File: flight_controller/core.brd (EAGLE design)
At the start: 94 x 90 mm, 103 parts, among them J1 M02, J13 MOLEX-3POS, J14 MOLEX-3POS, J15 MOLEX-4POS, J16 MOLEX-3POS, J17 M03, J18 M04, J19 MOLEX-3POS, J2 MOLEX-2POS, J20 MOLEX-4POS, J3 MOLEX-2POS, J4 MOLEX-2POS, J5 MOLEX-2POS, J6 MOLEX-2POS, J7 MOLEX-2POS, J8 MOLEX-2POS, J9 MOLEX-2POS, Q10 EM6K1, Q11 EM6K1, Q2 200mA/50V, Q5 200mA/50V, Q6 200mA/50V, Q7 EM6K1, Q8 EM6K1, U1 MPU-6000QFN-24, U2 MEAS-MS5611, U3 USD-SOCKETNEW, U4 STM32F405, U5 MIC5219 3.3V, Y1 16MHz

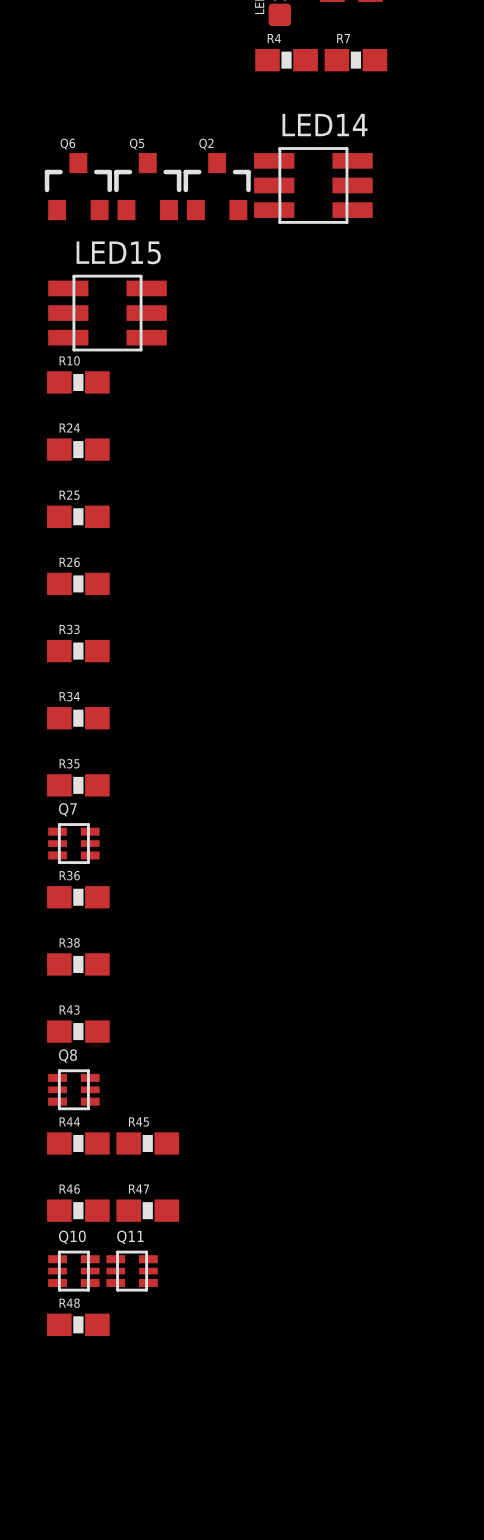
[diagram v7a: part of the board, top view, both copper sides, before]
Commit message: Replace LED MOSFETs with dual-channel MOSFETs.
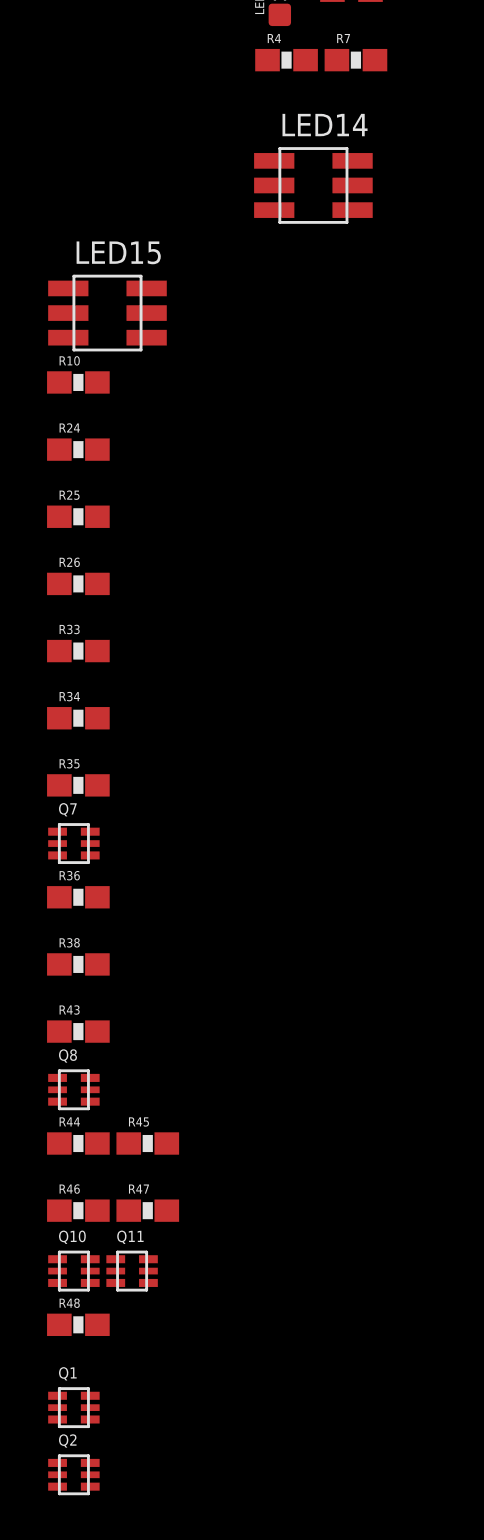
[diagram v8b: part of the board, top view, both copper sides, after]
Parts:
- removed Q5, Q6: 200mA/50V, SparkFun-DiscreteSemi:SOT23-3
- added Q1: EM6K1, OSURC_DiscreteSemi:SOT-666
- Q2: value 200mA/50V -> EM6K1; device SparkFun-DiscreteSemi:SOT23-3 -> OSURC_DiscreteSemi:SOT-666
- moved Q2 57.9 mm to (-224.0, -588.9)
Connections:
- net GND: now also Q1.1, Q1.4, Q2.1; no longer Q2.2, Q5.2, Q6.2
- net N$5: now also Q1.6; no longer Q2.3
- net N$6: now also Q1.3; no longer Q5.3
- net N$7: now also Q2.6; no longer Q6.3
- net TIM3-CH2-STSB: now also Q1.2; no longer Q2.1
- net TIM3-CH3-STSG: now also Q1.5; no longer Q5.1
- net TIM3-CH4-STSR: now also Q2.2; no longer Q6.1
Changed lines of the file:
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@@
 <attribute name="DIGIKEY_PN" value="475-2899-1-ND" x="-213.3" y="-531.3" size="1.778" layer="27" display="off"/>
-</element>
-<element name="Q2" library="SparkFun-DiscreteSemi" package="SOT23-3" value="200mA/50V" x="-217.6" y="-531.4">
-<attribute name="PROD_ID" value="TRANS-00830" x="-217.6" y="-531.4" size="1.778" layer="27" display="off"/>
-</element>
-<element name="Q5" library="SparkFun-DiscreteSemi" package="SOT23-3" value="200mA/50V" x="-220.7" y="-531.4">
-<attribute name="PROD_ID" value="TRANS-00830" x="-220.7" y="-531.4" size="1.778" layer="27" display="off"/>
-</element>
-<element name="Q6" library="SparkFun-DiscreteSemi" package="SOT23-3" value="200mA/50V" x="-223.8" y="-531.4">
-<attribute name="PROD_ID" value="TRANS-00830" x="-223.8" y="-531.4" size="1.778" layer="27" display="off"/>
 </element>
 <element name="LED15" library="OSURC_LED" package="PLCC-6" value="OSRAM-MULTILED-RGB" x="-222.5" y="-537">
@@
 </element>
 <element name="R48" library="SparkFun" package="0603-RES" value="1K" x="-223.8" y="-582.2"/>
+<element name="Q1" library="OSURC_DiscreteSemi" package="SOT-666" value="EM6K1" x="-224" y="-585.9">
+<attribute name="DIGIKEY_PN" value="EM6K1T2RCT-ND" x="-224" y="-585.9" size="1.778" layer="27" display="off"/>
+</element>
+<element name="Q2" library="OSURC_DiscreteSemi" package="SOT-666" value="EM6K1" x="-224" y="-588.9">
+<attribute name="DIGIKEY_PN" value="EM6K1T2RCT-ND" x="-224" y="-588.9" size="1.778" layer="27" display="off"/>
+</element>
 </elements>
 <signals>
@@
 <contactref element="LED6" pad="C"/>
 <contactref element="LED7" pad="C"/>
-<contactref element="Q2" pad="2"/>
-<contactref element="Q5" pad="2"/>
-<contactref element="Q6" pad="2"/>
 <contactref element="Q7" pad="1"/>
 <contactref element="Q7" pad="4"/>
@@
 <contactref element="Q11" pad="1"/>
 <contactref element="Q11" pad="4"/>
+<contactref element="Q1" pad="1"/>
+<contactref element="Q1" pad="4"/>
+<contactref element="Q2" pad="1"/>
 <wire x1="-127.4" y1="-372.6" x2="-136" y2="-372.6" width="0" layer="19" extent="1-1"/>
 <wire x1="-153.2" y1="-372.6" x2="-136" y2="-372.6" width="0" layer="19" extent="1-1"/>
@@
 <wire x1="-214.8" y1="-518.823" x2="-211.9" y2="-518.823" width="0" layer="19" extent="1-1"/>
 <wire x1="-214.8" y1="-521.923" x2="-214.8" y2="-518.823" width="0" layer="19" extent="1-1"/>
-<wire x1="-216.65" y1="-532.4" x2="-214.8" y2="-521.923" width="0" layer="19" extent="1-1"/>
-<wire x1="-219.75" y1="-532.4" x2="-216.65" y2="-532.4" width="0" layer="19" extent="1-1"/>
-<wire x1="-222.85" y1="-532.4" x2="-219.75" y2="-532.4" width="0" layer="19" extent="1-1"/>
 <wire x1="-212.1" y1="-499.9" x2="-207.5" y2="-514.2" width="0" layer="19" extent="1-1"/>
 <wire x1="-100.4" y1="-372.6" x2="-127.4" y2="-372.6" width="0" layer="19" extent="1-1"/>
@@
 <wire x1="-37.4" y1="-350.45" x2="-42.7" y2="-353.1" width="0" layer="19" extent="1-1"/>
 <wire x1="-34.7" y1="-353.1" x2="-37.4" y2="-350.45" width="0" layer="19" extent="1-1"/>
-<wire x1="-224.73" y1="-560.17" x2="-222.85" y2="-532.4" width="0" layer="19" extent="1-1"/>
+<wire x1="-224.73" y1="-560.17" x2="-214.8" y2="-521.923" width="0" layer="19" extent="1-1"/>
 <wire x1="-223.27" y1="-561.23" x2="-224.73" y2="-560.17" width="0" layer="19" extent="1-1"/>
 <wire x1="-224.73" y1="-571.17" x2="-223.27" y2="-561.23" width="0" layer="19" extent="1-1"/>
@@
 <wire x1="-224.73" y1="-579.27" x2="-223.27" y2="-580.33" width="0" layer="19" extent="1-1"/>
 <wire x1="-220.67" y1="-580.33" x2="-222.13" y2="-579.27" width="0" layer="19" extent="1-1"/>
+<wire x1="-224.73" y1="-585.37" x2="-223.27" y2="-580.33" width="0" layer="19" extent="1-1"/>
+<wire x1="-223.27" y1="-586.43" x2="-224.73" y2="-585.37" width="0" layer="19" extent="1-1"/>
+<wire x1="-224.73" y1="-588.37" x2="-223.27" y2="-586.43" width="0" layer="19" extent="1-1"/>
 <wire x1="-36.2" y1="-212.723" x2="-37.4" y2="-350.45" width="0" layer="19" extent="1-1"/>
 <wire x1="-33.3" y1="-209.623" x2="-36.2" y2="-212.723" width="0" layer="19" extent="1-1"/>
@@
 <signal name="TIM3-CH3-STSG">
 <contactref element="U4" pad="26"/>
-<contactref element="Q5" pad="1"/>
-<wire x1="-4.7" y1="-161.9" x2="-221.65" y2="-532.4" width="0" layer="19" extent="1-1"/>
+<contactref element="Q1" pad="5"/>
+<wire x1="-223.27" y1="-585.9" x2="-4.7" y2="-161.9" width="0" layer="19" extent="1-1"/>
 </signal>
 <signal name="TIM3-CH1">
@@
 <signal name="N$5">
 <contactref element="LED15" pad="C1"/>
-<contactref element="Q2" pad="3"/>
 <contactref element="LED14" pad="C1"/>
-<wire x1="-217.6" y1="-530.3" x2="-224.25" y2="-535.9" width="0" layer="19" extent="1-1"/>
-<wire x1="-215.05" y1="-530.2" x2="-217.6" y2="-530.3" width="0" layer="19" extent="1-1"/>
+<contactref element="Q1" pad="6"/>
+<wire x1="-215.05" y1="-530.2" x2="-224.25" y2="-535.9" width="0" layer="19" extent="1-1"/>
+<wire x1="-223.27" y1="-585.37" x2="-224.25" y2="-535.9" width="0" layer="19" extent="1-1"/>
 </signal>
 <signal name="N$6">
 <contactref element="LED15" pad="C3"/>
-<contactref element="Q5" pad="3"/>
 <contactref element="LED14" pad="C3"/>
-<wire x1="-220.7" y1="-530.3" x2="-224.25" y2="-538.1" width="0" layer="19" extent="1-1"/>
-<wire x1="-215.05" y1="-532.4" x2="-220.7" y2="-530.3" width="0" layer="19" extent="1-1"/>
+<contactref element="Q1" pad="3"/>
+<wire x1="-215.05" y1="-532.4" x2="-224.25" y2="-538.1" width="0" layer="19" extent="1-1"/>
+<wire x1="-224.73" y1="-586.43" x2="-224.25" y2="-538.1" width="0" layer="19" extent="1-1"/>
 </signal>
 <signal name="N$7">
 <contactref element="LED15" pad="C2"/>
-<contactref element="Q6" pad="3"/>
 <contactref element="LED14" pad="C2"/>
-<wire x1="-223.8" y1="-530.3" x2="-224.25" y2="-537" width="0" layer="19" extent="1-1"/>
-<wire x1="-215.05" y1="-531.3" x2="-223.8" y2="-530.3" width="0" layer="19" extent="1-1"/>
+<contactref element="Q2" pad="6"/>
+<wire x1="-215.05" y1="-531.3" x2="-224.25" y2="-537" width="0" layer="19" extent="1-1"/>
+<wire x1="-223.27" y1="-588.37" x2="-224.25" y2="-537" width="0" layer="19" extent="1-1"/>
 </signal>
 <signal name="N$8">
@@
 <contactref element="R34" pad="2"/>
 <wire x1="-222.95" y1="-555.1" x2="-220.75" y2="-535.9" width="0" layer="19" extent="1-1"/>
-</signal>
-<signal name="TIM3-CH2-STSB">
-<contactref element="Q2" pad="1"/>
-</signal>
-<signal name="TIM3-CH4-STSR">
-<contactref element="Q6" pad="1"/>
 </signal>
 <signal name="KILL1">
@@
 <wire x1="-220.67" y1="-579.8" x2="-222.13" y2="-579.8" width="0" layer="19" extent="1-1"/>
 </signal>
+<signal name="TIM3-CH2-STSB">
+<contactref element="Q1" pad="2"/>
+</signal>
+<signal name="TIM3-CH4-STSR">
+<contactref element="Q2" pad="2"/>
+</signal>
 </signals>
